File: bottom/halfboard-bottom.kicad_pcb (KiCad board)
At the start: 4 copper layers, 117.4 x 87.9 mm, 0 parts

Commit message: move gerber files to a folder
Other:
- copper layers 4 -> 2
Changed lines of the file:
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@@
-(kicad_pcb (version 20171130) (host pcbnew 5.1.9)
+(kicad_pcb (version 20171130) (host pcbnew "(5.1.8-0-10_14)")
   (general
     (thickness 1.6)
@@
   (layers
     (0 F.Cu signal)
-    (1 In1.Cu signal)
-    (2 In2.Cu signal)
     (31 B.Cu signal)
     (32 B.Adhes user)
@@
     (43 Eco2.User user)
     (44 Edge.Cuts user)
+    (45 Margin user)
+    (46 B.CrtYd user)
+    (47 F.CrtYd user)
+    (48 B.Fab user)
+    (49 F.Fab user)
   )
   (setup
@@
     (visible_elements FFFFF7FF)
     (pcbplotparams
-      (layerselection 0x01fff_ffffffff)
+      (layerselection 0x3ffff_ffffffff)
       (usegerberextensions false)
       (usegerberattributes false)
@@
       (drillshape 0)
       (scaleselection 1)
-      (outputdirectory ""))
+      (outputdirectory "gbr/"))
   )
   (net 0 "")

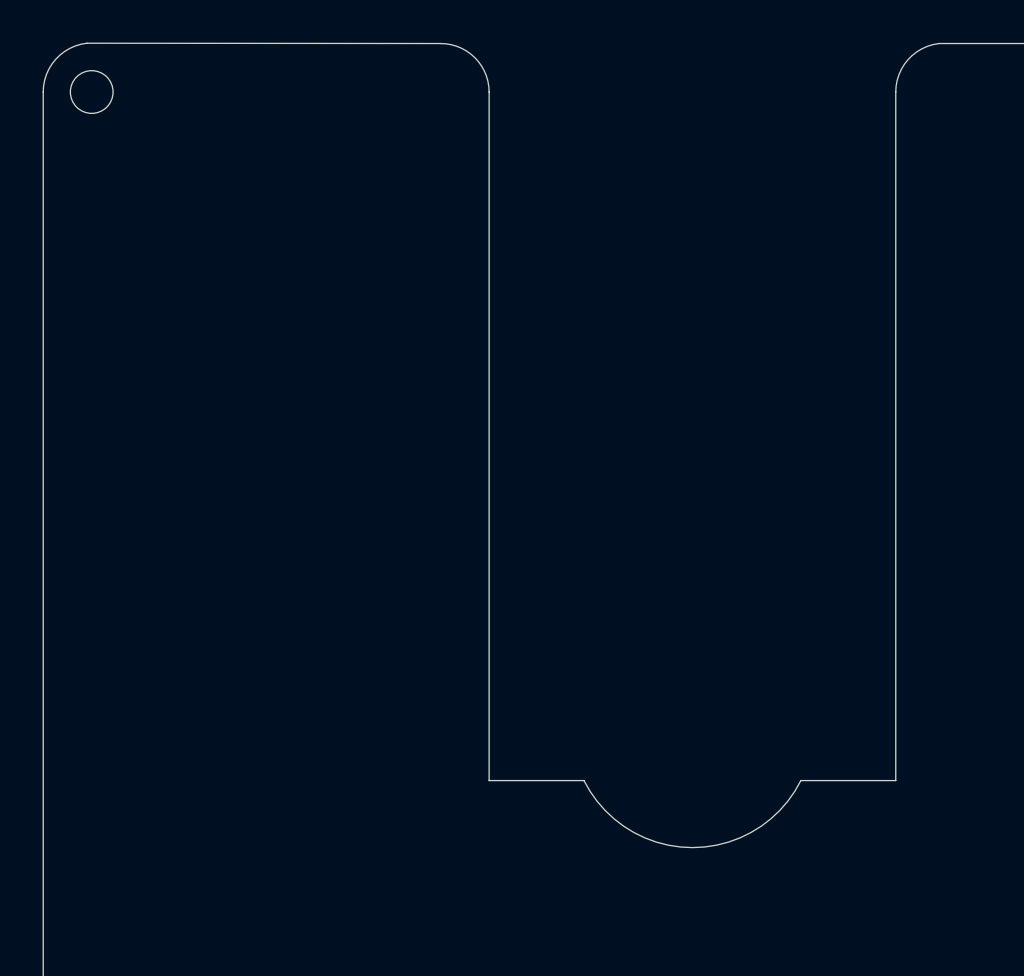
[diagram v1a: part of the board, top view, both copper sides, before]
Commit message: 5x4 layout instead of 6x4
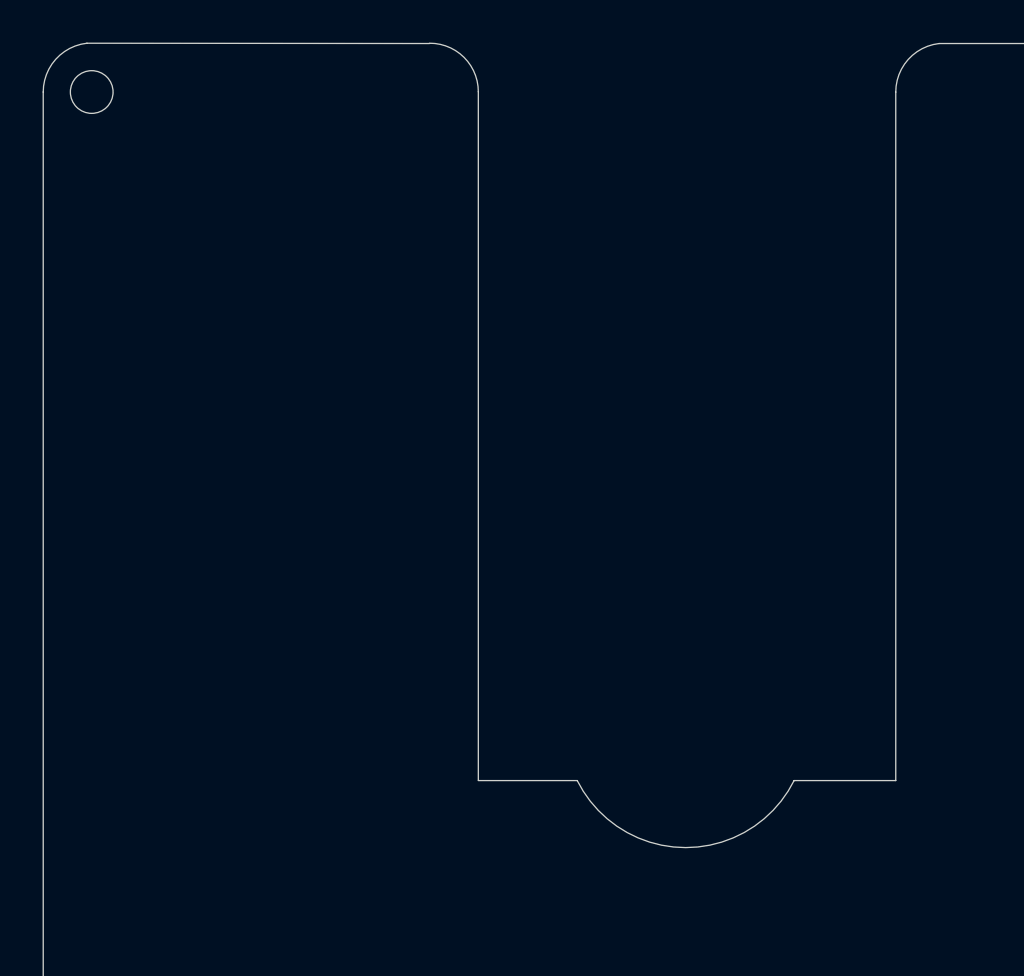
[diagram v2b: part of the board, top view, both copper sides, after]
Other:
- outline, holes or cut-outs redrawn
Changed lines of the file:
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@@
     (effects (font (size 1 1) (thickness 0.15)))
   )
-  (gr_line (start 64.77 83.82) (end 69.215 83.82) (layer Edge.Cuts) (width 0.05))
-  (gr_arc (start 74.295 81.28) (end 69.215 83.82) (angle -126.8698976) (layer Edge.Cuts) (width 0.05))
+  (gr_line (start 64.262 83.82) (end 68.8975 83.82) (layer Edge.Cuts) (width 0.05))
+  (gr_arc (start 73.9775 81.28) (end 68.8975 83.82) (angle -126.8698976) (layer Edge.Cuts) (width 0.05))
   (gr_circle (center 102.65 51.562) (end 103.65 51.562) (layer Edge.Cuts) (width 0.05))
   (gr_arc (start 86.106042 51.562) (end 85.852043 49.29011) (angle -83.70000491) (layer Edge.Cuts) (width 0.05))
   (gr_line (start 158.99002 49.29011) (end 85.852043 49.29011) (layer Edge.Cuts) (width 0.05))
-  (gr_arc (start 62.498067 51.562) (end 64.77 51.562) (angle -90.40000105) (layer Edge.Cuts) (width 0.05))
+  (gr_arc (start 61.991861 51.547878) (end 64.263794 51.547878) (angle -90.40000105) (layer Edge.Cuts) (width 0.05))
   (gr_line (start 83.82 83.82) (end 83.82 51.565161) (layer Edge.Cuts) (width 0.05))
-  (gr_line (start 79.375 83.82) (end 83.82 83.82) (layer Edge.Cuts) (width 0.05))
-  (gr_line (start 64.77 51.562) (end 64.77 83.82) (layer Edge.Cuts) (width 0.05))
+  (gr_line (start 79.0575 83.82) (end 83.82 83.82) (layer Edge.Cuts) (width 0.05))
+  (gr_line (start 64.263794 51.547878) (end 64.263794 83.805878) (layer Edge.Cuts) (width 0.05))
   (gr_circle (center 158.75 94.742) (end 159.75 94.742) (layer Edge.Cuts) (width 0.05))
   (gr_line (start 46.167795 137.14391) (end 158.992054 137.168666) (layer Edge.Cuts) (width 0.05))
   (gr_line (start 161.277967 134.896777) (end 161.275933 51.561999) (layer Edge.Cuts) (width 0.05))
-  (gr_line (start 62.482206 49.290122) (end 45.926068 49.276002) (layer Edge.Cuts) (width 0.05))
+  (gr_line (start 61.976 49.290122) (end 45.926068 49.276002) (layer Edge.Cuts) (width 0.05))
   (gr_line (start 43.88 51.562001) (end 43.88 134.872033) (layer Edge.Cuts) (width 0.05))
   (gr_arc (start 46.180067 51.562001) (end 45.926068 49.276002) (angle -83.65983026) (layer Edge.Cuts) (width 0.05))
